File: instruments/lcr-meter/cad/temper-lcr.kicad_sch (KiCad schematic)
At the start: 0 parts

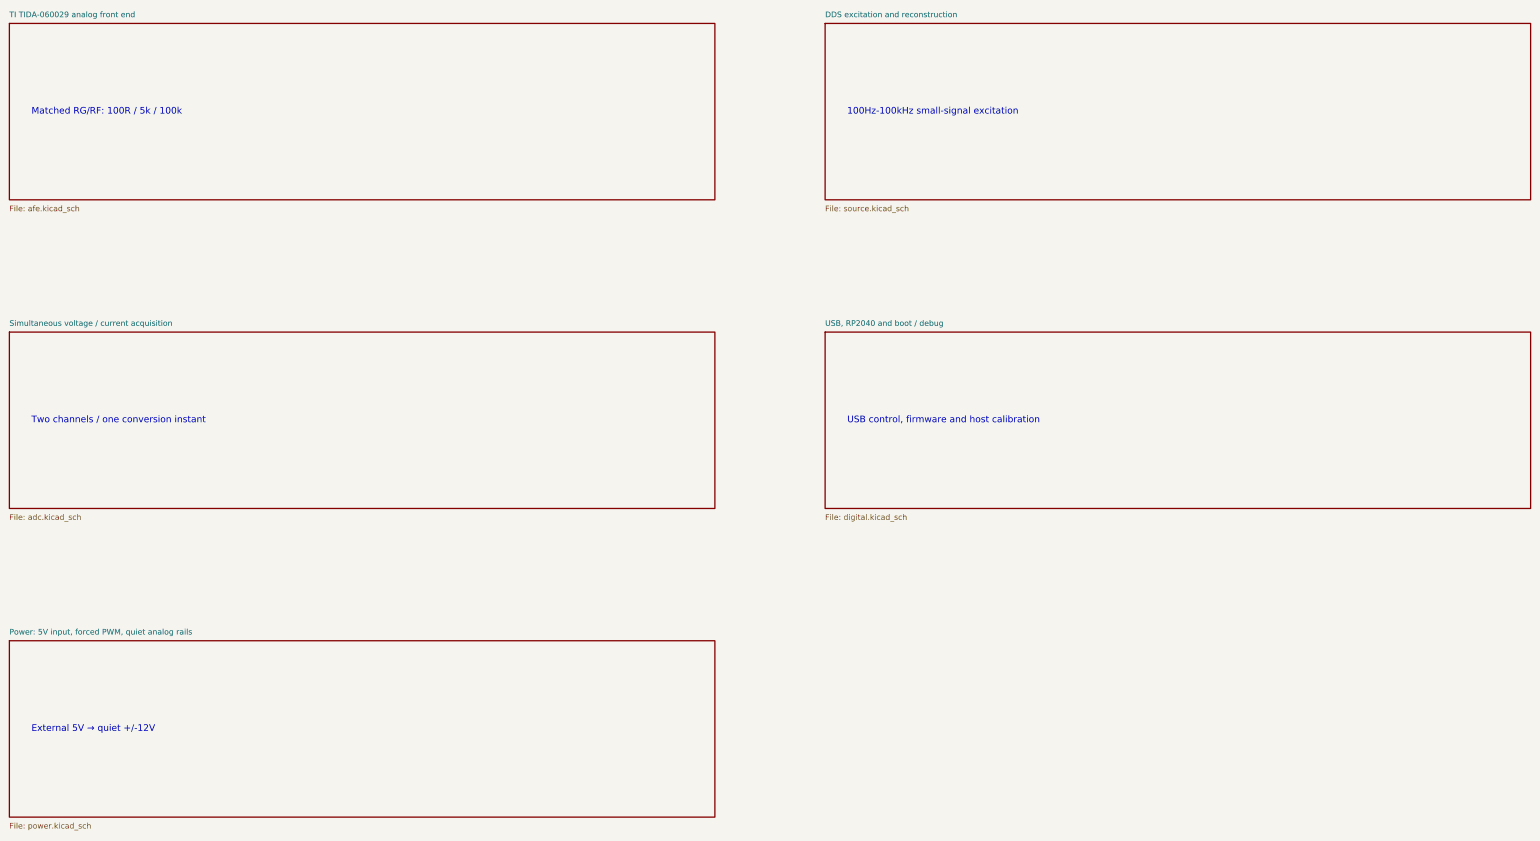
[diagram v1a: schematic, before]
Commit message: feat(lcr): Rev E board with TAC5112 codec front end and relay ranges
Hand-routed Rev E on the Rev D outline:
- removes the ADS9224R, AD9833, both THS4551s, FB2 and JP1-JP6;
- adds the TAC5112 with its own AP2112K for 3V3A, three TQ2SA latching
  relays and their AO3400A drivers.

cad/tools/rev_e.py builds design.json and routing.json from the Rev D
package. rev_e_routes.py gives every new segment and via by coordinate.

Details:
- Every via is now a 0.3 mm drill with a pad of 0.45 mm or more.
  The board rules set a 0.30 mm minimum hole and a 0.075 mm minimum
  annular ring.
- Basic-library swaps: D1 is now SRV05-4, and SW1/SW2 are now TS-1088.
- placement_offsets.py adds JLC CPL offsets for the new keyed parts,
  read from the lceda.cn EasyEDA mirror (easyeda.com returns 403). It
  reproduces the audited offsets for U3 (270) and Q1 (180).

Checks:
- rebuild.sh: ERC 0, DRC 0 violations and 0 unconnected, parity 0.
- package_cad and audit_dfm pass: 34 intended via-in-pad, none
  unexpected.
- independent_check.py e: 575 pins, 0 findings.

Co-Authored-By: Claude Opus 5.5 <noreply@anthropic.com>
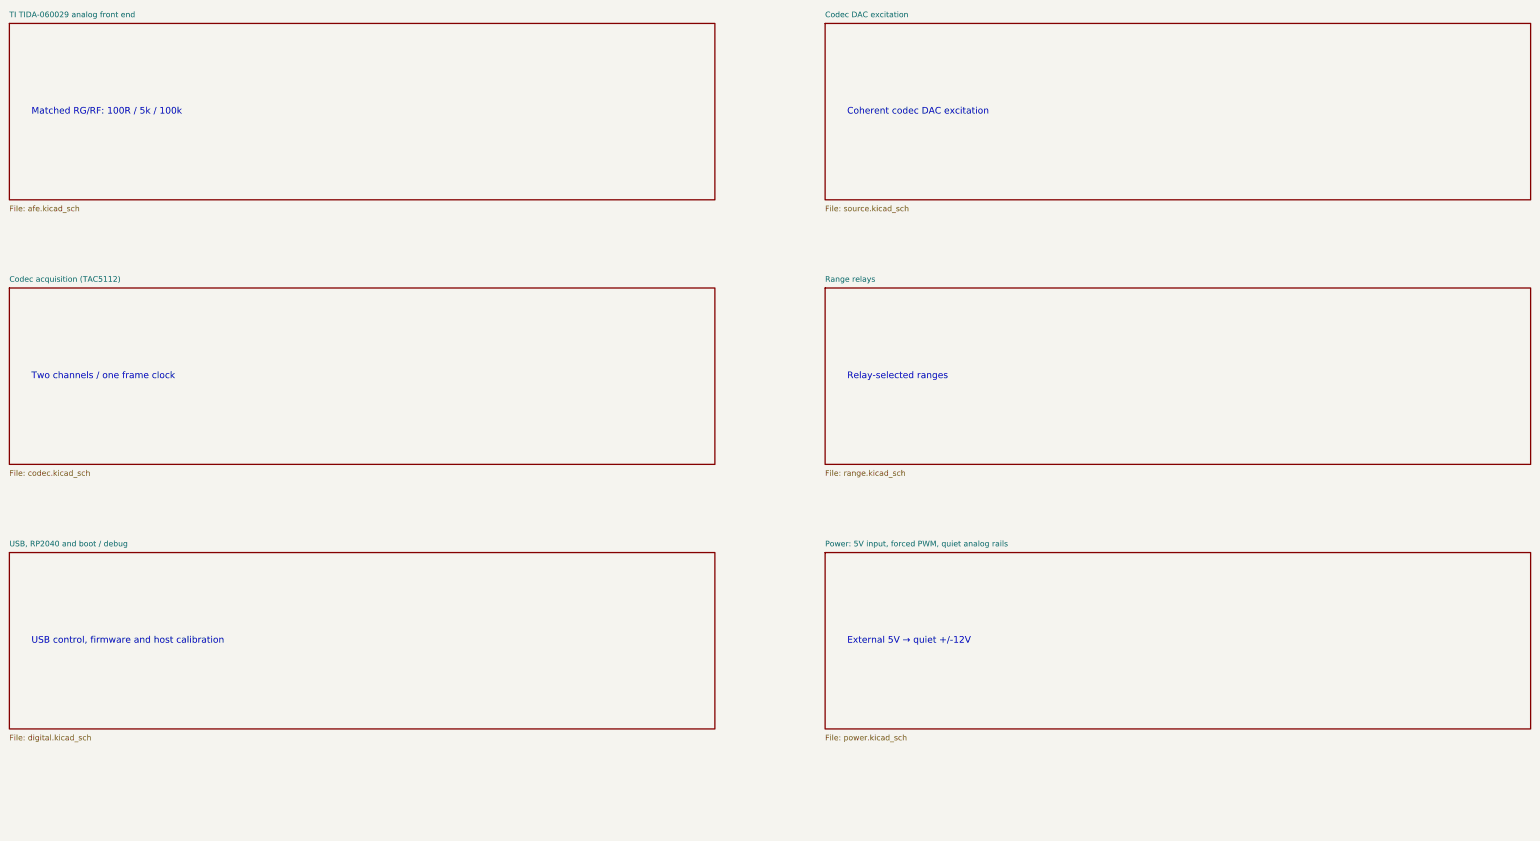
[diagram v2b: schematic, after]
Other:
- sheet DDS excitation and reconstruction renamed Codec DAC excitation
- removed sheet Simultaneous voltage / current acquisition
- added sheet Codec acquisition (TAC5112) (codec.kicad_sch)
- added sheet Range relays (range.kicad_sch)
- note added: "Coherent codec DAC excitation"
- note added: "Relay-selected ranges"
- note added: "Two channels / one frame clock"
- note removed: "100Hz-100kHz small-signal excitation"
- note removed: "Two channels / one conversion instant"
